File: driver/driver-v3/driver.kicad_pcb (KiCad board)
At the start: 4 copper layers, 98 x 34 mm, 40 parts, among them J1 Conn_02x08_Odd_Even_Male, J2 Conn_02x08_Odd_Even_Female, J3 Conn_01x05, J4 Conn_01x03_Pin, J5 Conn_01x05, J6 Conn_01x03_Pin, U1 DRV8804PWP, U2 SN74HCS165DYYR, U3 DRV8804PWP

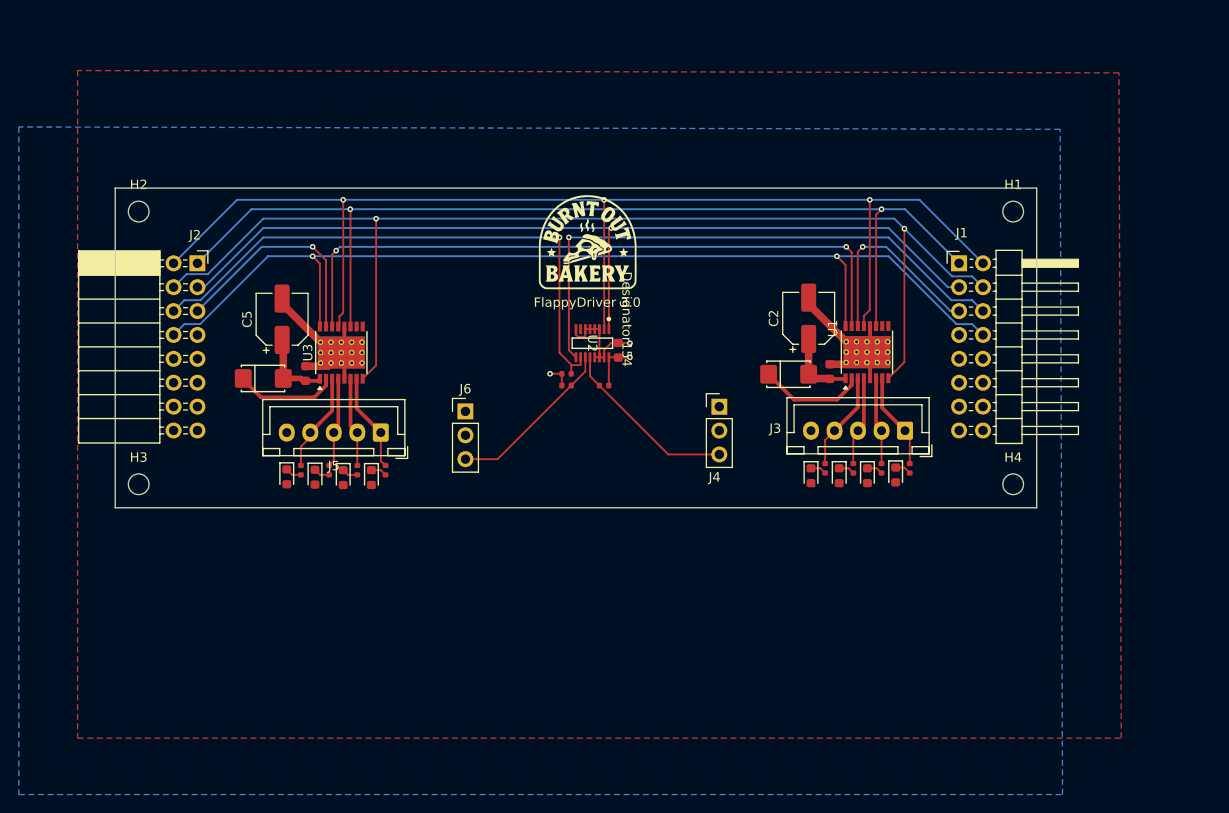
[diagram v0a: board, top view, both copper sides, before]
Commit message: Optimize driver3 size and re-add spin test to firmware.
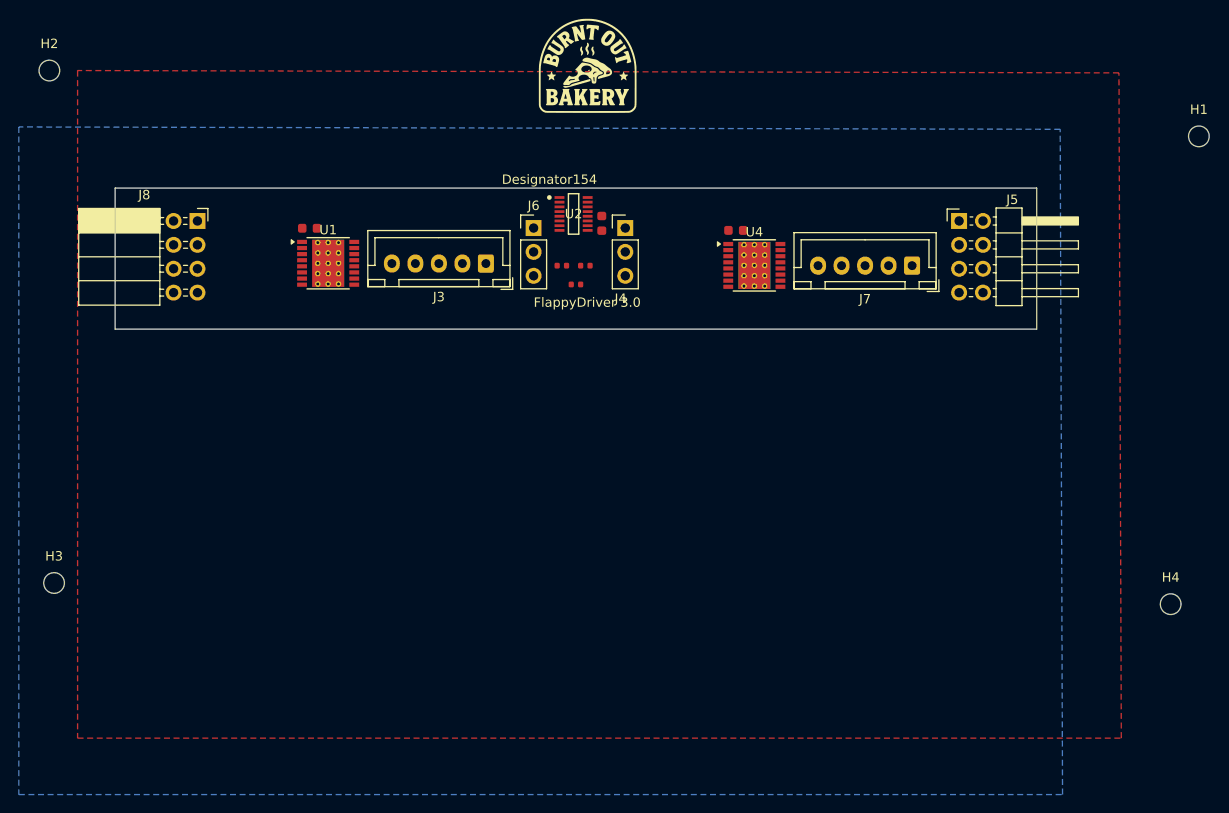
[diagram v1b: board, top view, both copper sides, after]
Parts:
- removed C2, C5: C_Polarized, Capacitor_SMD:CP_Elec_5x5.4
- removed C4: 100nF, PCM_JLCPCB:C_0603
- removed D1, D6: 1SMA4749A, PCM_JLCPCB:D_DO-214AC(SMA)
- removed D10, D2, D3, D4, D5, D7, D8, D9: Red, PCM_JLCPCB:D_0603
- removed J1: Conn_02x08_Odd_Even_Male, Connector_PinHeader_2.54mm:PinHeader_2x08_P2.54mm_Horizontal
- removed J2: Conn_02x08_Odd_Even_Female, Connector_PinSocket_2.54mm:PinSocket_2x08_P2.54mm_Horizontal
- removed R1, R10, R2, R3, R4, R7, R8, R9: 10kΩ, PCM_JLCPCB:R_0402
- removed U3: DRV8804PWP, Package_SO:HTSSOP-16-1EP_4.4x5mm_P0.65mm_EP3.4x5mm_Mask3x3mm_ThermalVias
- added C6: 100nF, PCM_JLCPCB:C_0603, F.Cu at (166.0, 54.5)
- added J7: Conn_01x05, Connector_JST:JST_XH_B5B-XH-A_1x05_P2.50mm_Vertical, F.Cu at (184.8, 58.2)
- added J8: Conn_02x04_Odd_Even_Female, Connector_PinSocket_2.54mm:PinSocket_2x04_P2.54mm_Horizontal, F.Cu at (108.8, 53.5)
- added U4: DRV8804PWP, Package_SO:HTSSOP-16-1EP_4.4x5mm_P0.65mm_EP3.4x5mm_Mask3x3mm_ThermalVias, F.Cu at (168.0, 58.2)
- J5: value Conn_01x05 -> Conn_02x04_Odd_Even_Male; footprint Connector_JST:JST_XH_B5B-XH-A_1x05_P2.50mm_Vertical -> Connector_PinHeader_2.54mm:PinHeader_2x04_P2.54mm_Horizontal
- moved J5 65.5 mm to (189.8, 53.5), turned to 0 degrees
- moved U1 58.1 mm to (122.7, 58.0), turned to 0 degrees
- moved C1 57.4 mm to (120.7, 54.3), turned to 0 degrees
- moved J3 48.0 mm to (139.4, 58.0)
- moved J4 21.5 mm to (154.2, 54.2)
- moved H1 21.3 mm to (215.2, 44.5)
- moved H4 21.1 mm to (212.2, 94.2)
- moved J6 20.8 mm to (144.5, 54.2)
- moved G1 18.8 mm to (150.2, 37.5)
- moved H2 17.8 mm to (93.0, 37.5)
- moved U2 13.9 mm to (148.8, 52.7), turned to 0 degrees
- moved H3 13.8 mm to (93.5, 92.0)
- moved C3 13.6 mm to (151.8, 53.8)
- moved R5 12.9 mm to (150.0, 58.2)
- moved R6 11.5 mm to (147.5, 58.2)
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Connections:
- J5 pad 1: Net-(J5-Pin_1) -> GND
- J5 pad 2: Net-(J5-Pin_2) -> CIPO1
- J5 pad 3: Net-(J5-Pin_3) -> LL
- J5 pad 4: Net-(J5-Pin_4) -> SCLK
- J5 pad 5: +12V -> COPI1
- U1 pad 14: COPI1 -> COPI2
- U1 pad 15: COPI2 -> COPI3
- U1 pad 2: Net-(U1-VCLAMP) -> +12V
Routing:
- net SCLK: track 132.8 -> 0.00 mm, vias 3 -> 0
- net NENBL: track 126.3 -> 0.00 mm, vias 2 -> 0
- net LATCH: track 110.9 -> 0.00 mm, vias 2 -> 0
- net FAULT: track 108.6 -> 0.00 mm, vias 2 -> 0
- net LOAD: track 97.1 -> 0.00 mm, vias 1 -> 0
- net COPI2: track 71.3 -> 0.00 mm, vias 2 -> 0
- net CIPO2: track 61.1 -> 0.00 mm, vias 1 -> 0
- net CIPO1: track 60.3 -> 0.00 mm, vias 1 -> 0
- net GND: track 45.1 -> 0.00 mm, vias 1 -> 0
- net COPI3: track 24.1 -> 0.00 mm, vias 1 -> 0
- net COPI1: track 21.7 -> 0.00 mm, vias 1 -> 0
- net Net-(J4-Pin_3): track 19.2 -> 0.00 mm
- net Net-(J6-Pin_3): track 18.1 -> 0.00 mm
- net +12V: track 16.2 -> 0.00 mm
- net Net-(U1-VCLAMP): track 11.3 -> 0.00 mm
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- removed copper zone on In2.Cu, net +3V3
- removed copper zone on In1.Cu, net GND
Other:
- board size 98 x 34 mm -> 98 x 15 mm
- copper layers 4 -> 2
